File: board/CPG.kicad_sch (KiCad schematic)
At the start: 21 parts, among them J1 MAINS, J2 VALVE, J3 PUMP, U1 PAN2110P0AA, U2 PY32F030F1xPx, U3 HLK-PM03, X1 SWD, Y1 16MHz

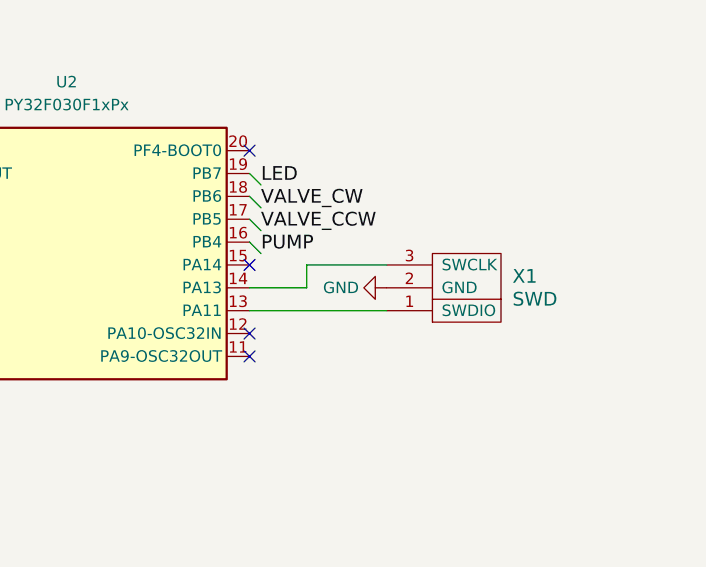
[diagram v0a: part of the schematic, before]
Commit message: Add CPG firmware and correct SWD header
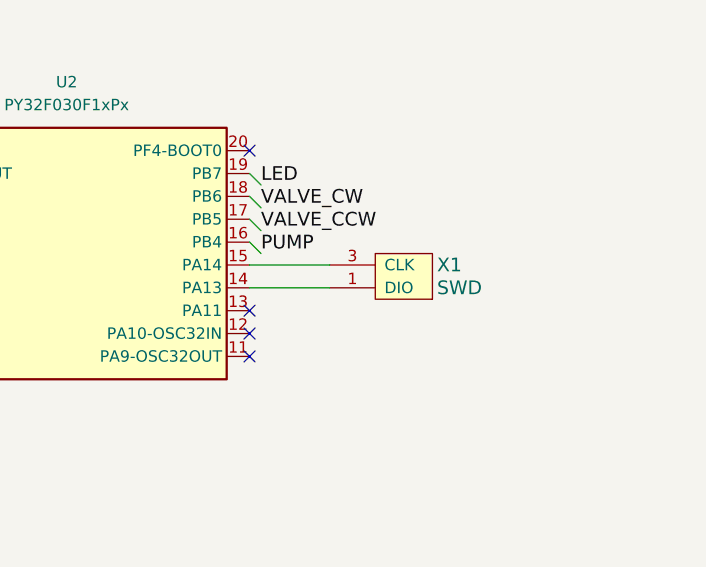
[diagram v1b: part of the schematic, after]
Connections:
- net at U2.13 (PA11): no longer X1.1 (SWDIO)
- net at U2.14 (PA13): now also X1.1 (DIO); no longer X1.3 (SWCLK)
- net at U2.15 (PA14): now also X1.3 (CLK)
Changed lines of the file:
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@@
 	)
 	(no_connect
+		(at 214.63 101.6)
+	)
+	(no_connect
 		(at 214.63 106.68)
 	)
@@
 		(at 214.63 104.14)
 	)
-	(no_connect
-		(at 214.63 96.52)
-	)
 	(wire
 		(pts
@@
 	(wire
 		(pts
-			(xy 214.63 101.6) (xy 229.87 101.6)
-		)
-		(stroke
-			(width 0)
-			(type default)
-		)
-	)
-	(wire
-		(pts
 			(xy 177.8 39.37) (xy 184.15 39.37)
 		)
@@
 	(wire
 		(pts
-			(xy 95.25 147.32) (xy 110.49 147.32)
+			(xy 214.63 96.52) (xy 223.52 96.52)
 		)
 		(stroke
@@
 	(wire
 		(pts
-			(xy 53.34 139.7) (xy 54.61 138.43)
+			(xy 95.25 147.32) (xy 110.49 147.32)
 		)
 		(stroke
@@
 	(wire
 		(pts
-			(xy 214.63 99.06) (xy 220.98 99.06)
+			(xy 53.34 139.7) (xy 54.61 138.43)
 		)
 		(stroke
@@
 	(wire
 		(pts
-			(xy 220.98 99.06) (xy 220.98 96.52)
-		)
-		(stroke
-			(width 0)
-			(type default)
-		)
-	)
-	(wire
-		(pts
-			(xy 220.98 96.52) (xy 229.87 96.52)
-		)
-		(stroke
-			(width 0)
-			(type default)
-		)
-	)
-	(wire
-		(pts
 			(xy 209.55 46.99) (xy 218.44 46.99)
 		)
@@
 		)
 	)
+	(wire
+		(pts
+			(xy 214.63 99.06) (xy 223.52 99.06)
+		)
+		(stroke
+			(width 0)
+			(type default)
+		)
+	)
 	(label "RF_SCK"
 		(at 111.76 107.95 0)
@@
 	(symbol
 		(lib_id "power:GND")
-		(at 229.87 99.06 270)
-		(unit 1)
-		(body_style 1)
-		(exclude_from_sim no)
-		(in_bom yes)
-		(on_board yes)
-		(in_pos_files yes)
-		(dnp no)
-		(property "Reference" "#PWR017"
-			(at 223.52 99.06 0)
-			(hide yes)
-			(show_name no)
-			(do_not_autoplace no)
-			(effects
-				(font
-					(size 1.27 1.27)
-				)
-			)
-		)
-		(property "Value" "GND"
-			(at 224.79 99.06 90)
-			(show_name no)
-			(do_not_autoplace no)
-			(effects
-				(font
-					(size 1.27 1.27)
-				)
-			)
-		)
-		(property "Footprint" ""
-			(at 229.87 99.06 0)
-			(hide yes)
-			(show_name no)
-			(do_not_autoplace no)
-			(effects
-				(font
-					(size 1.27 1.27)
-				)
-			)
-		)
-		(property "Datasheet" ""
-			(at 229.87 99.06 0)
-			(hide yes)
-			(show_name no)
-			(do_not_autoplace no)
-			(effects
-				(font
-					(size 1.27 1.27)
-				)
-			)
-		)
-		(property "Description" "Power symbol creates a global label with name \"GND\" , ground"
-			(at 229.87 99.06 0)
-			(hide yes)
-			(show_name no)
-			(do_not_autoplace no)
-			(effects
-				(font
-					(size 1.27 1.27)
-				)
-			)
-		)
-		(pin "1"
-		)
-		(instances
-			(project "CPG"
-				(path "/6b7dd4b9-634f-41b4-b846-9b2e2d6d43c6"
-					(reference "#PWR017")
-					(unit 1)
-				)
-			)
-		)
-	)
-	(symbol
-		(lib_id "power:GND")
 		(at 157.48 88.9 270)
 		(unit 1)
@@
 	(symbol
 		(lib_id "Drake:SWD")
-		(at 238.76 99.06 180)
+		(at 231.14 97.79 180)
 		(unit 1)
 		(body_style 1)
@@
 		(in_pos_files yes)
 		(dnp no)
-		(fields_autoplaced yes)
 		(property "Reference" "X1"
-			(at 243.84 97.7899 0)
+			(at 235.458 96.52 0)
 			(show_name no)
 			(do_not_autoplace no)
@@
 		)
 		(property "Value" "SWD"
-			(at 243.84 100.3299 0)
+			(at 235.458 99.06 0)
 			(show_name no)
 			(do_not_autoplace no)
@@
 		)
 		(property "Footprint" "Drake:SWD"
-			(at 238.76 90.17 0)
+			(at 231.14 88.9 0)
 			(hide yes)
 			(show_name no)
@@
 		)
 		(property "Datasheet" ""
-			(at 238.76 99.06 0)
+			(at 231.14 97.79 0)
 			(show_name no)
 			(do_not_autoplace no)
@@
 		)
 		(property "Description" ""
-			(at 238.76 99.06 0)
+			(at 231.14 97.79 0)
 			(hide yes)
 			(show_name no)
